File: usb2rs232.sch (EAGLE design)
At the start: 11 parts, among them U1 CP2101, U2 MAX232

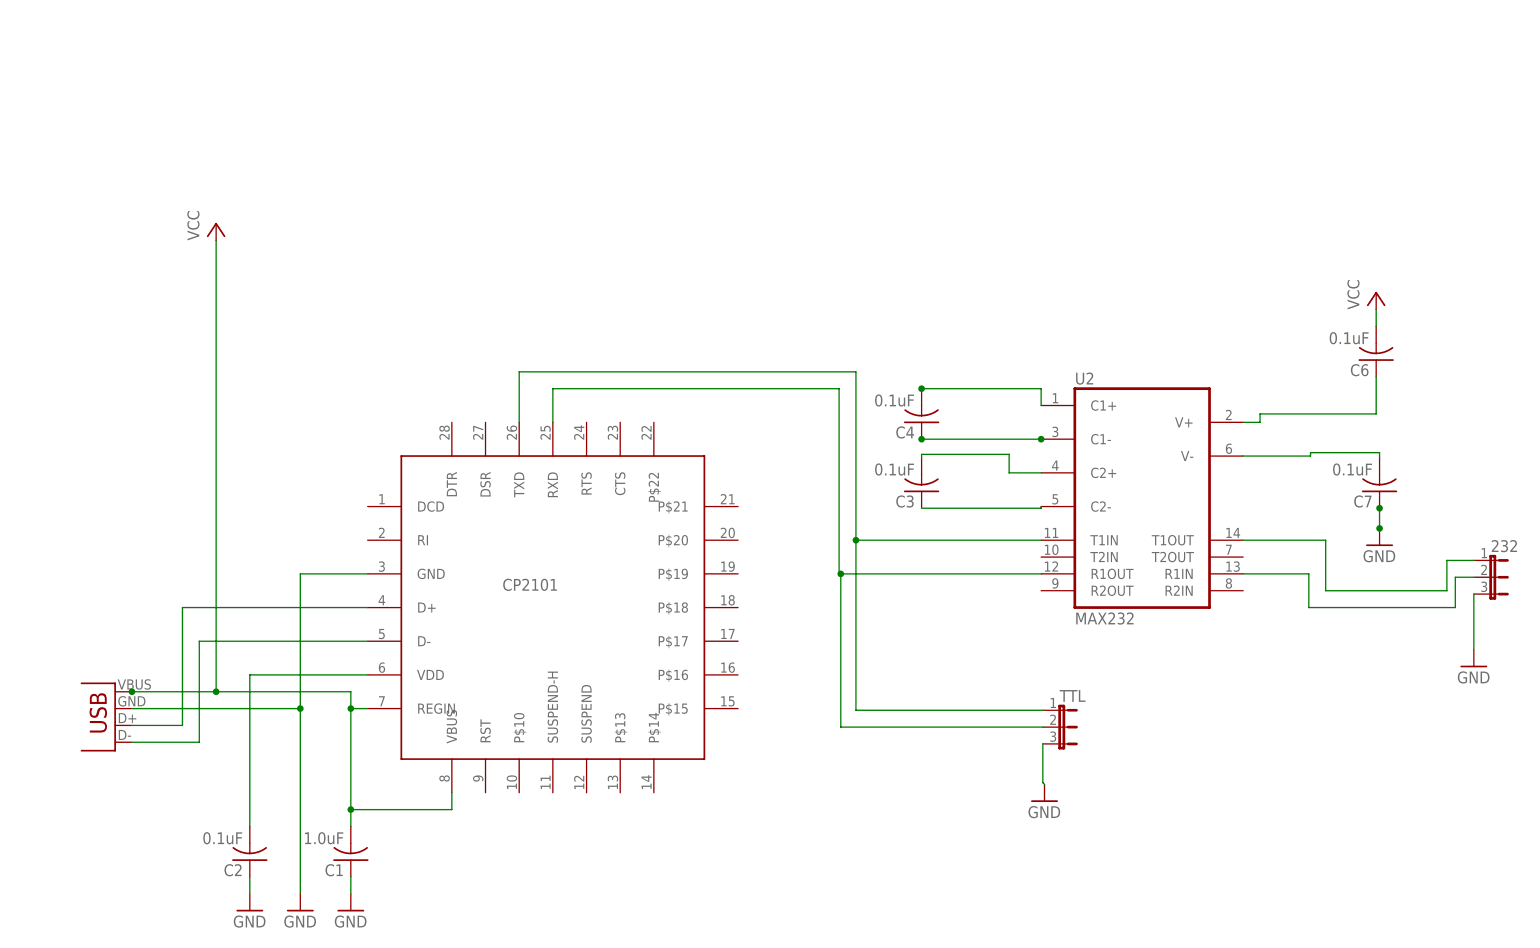
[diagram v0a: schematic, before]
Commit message: Fix CP2102 package issues
Change-Id: I1545ad8a51535be1dc4a5aefa6ad10a204795dc0
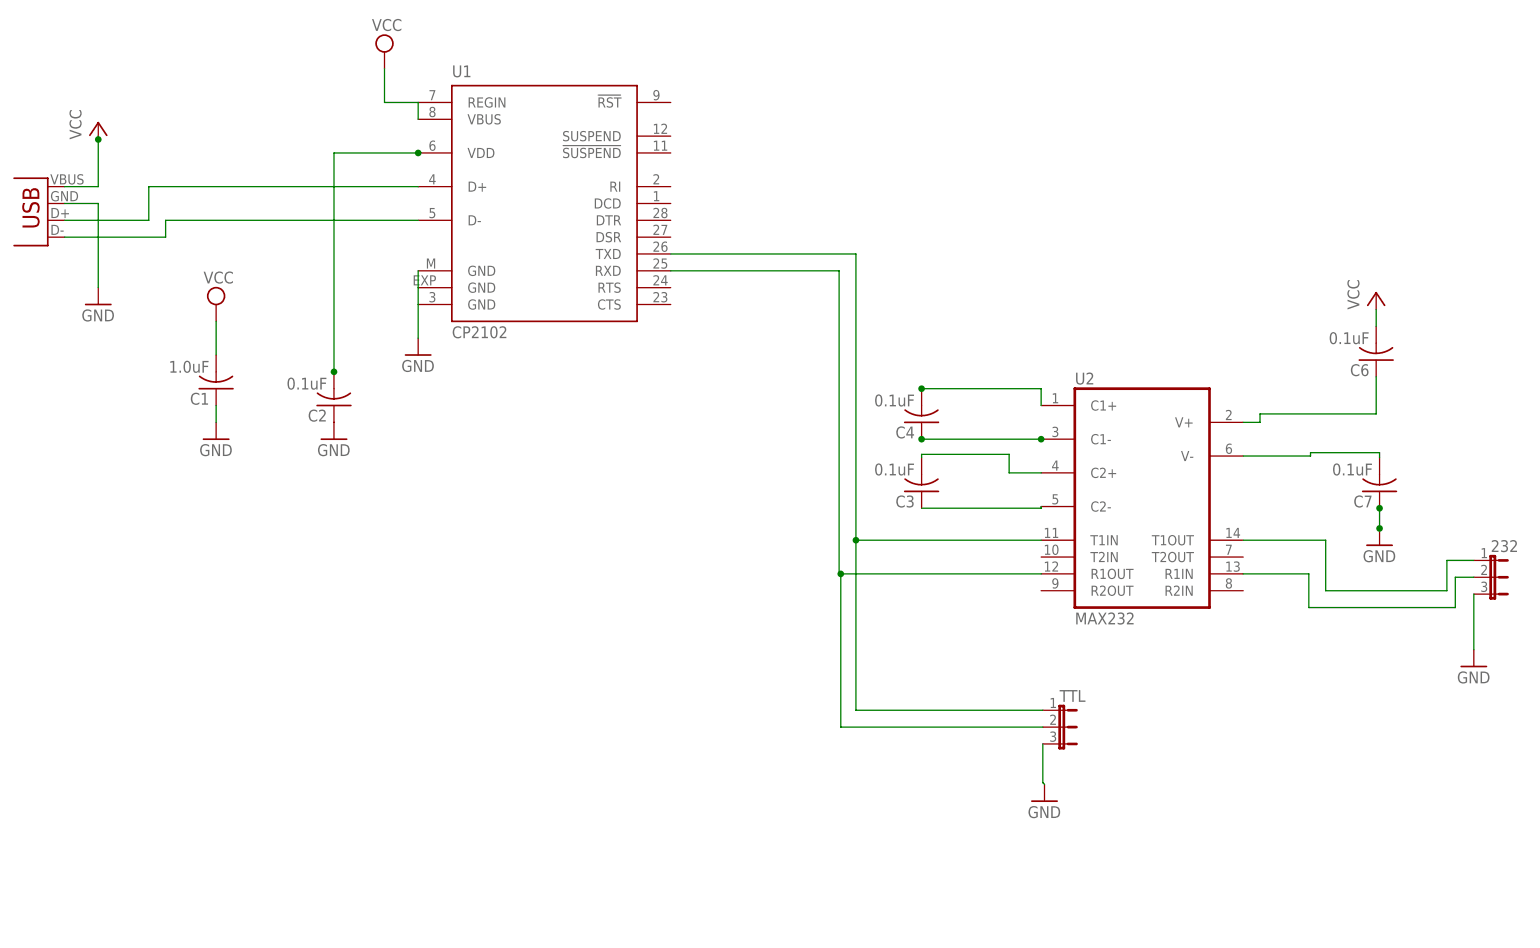
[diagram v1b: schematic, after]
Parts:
- U1: value CP2101 -> CP2102; device futz:CP2101 -> silabs:CP2102
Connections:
- net GND: now also U1.GND@EXP, U1.GND@M
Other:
- moved on the sheet: C1, C2
